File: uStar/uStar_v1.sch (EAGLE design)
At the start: 38 parts, among them IC1 INA138, X1 BU-SMA-V

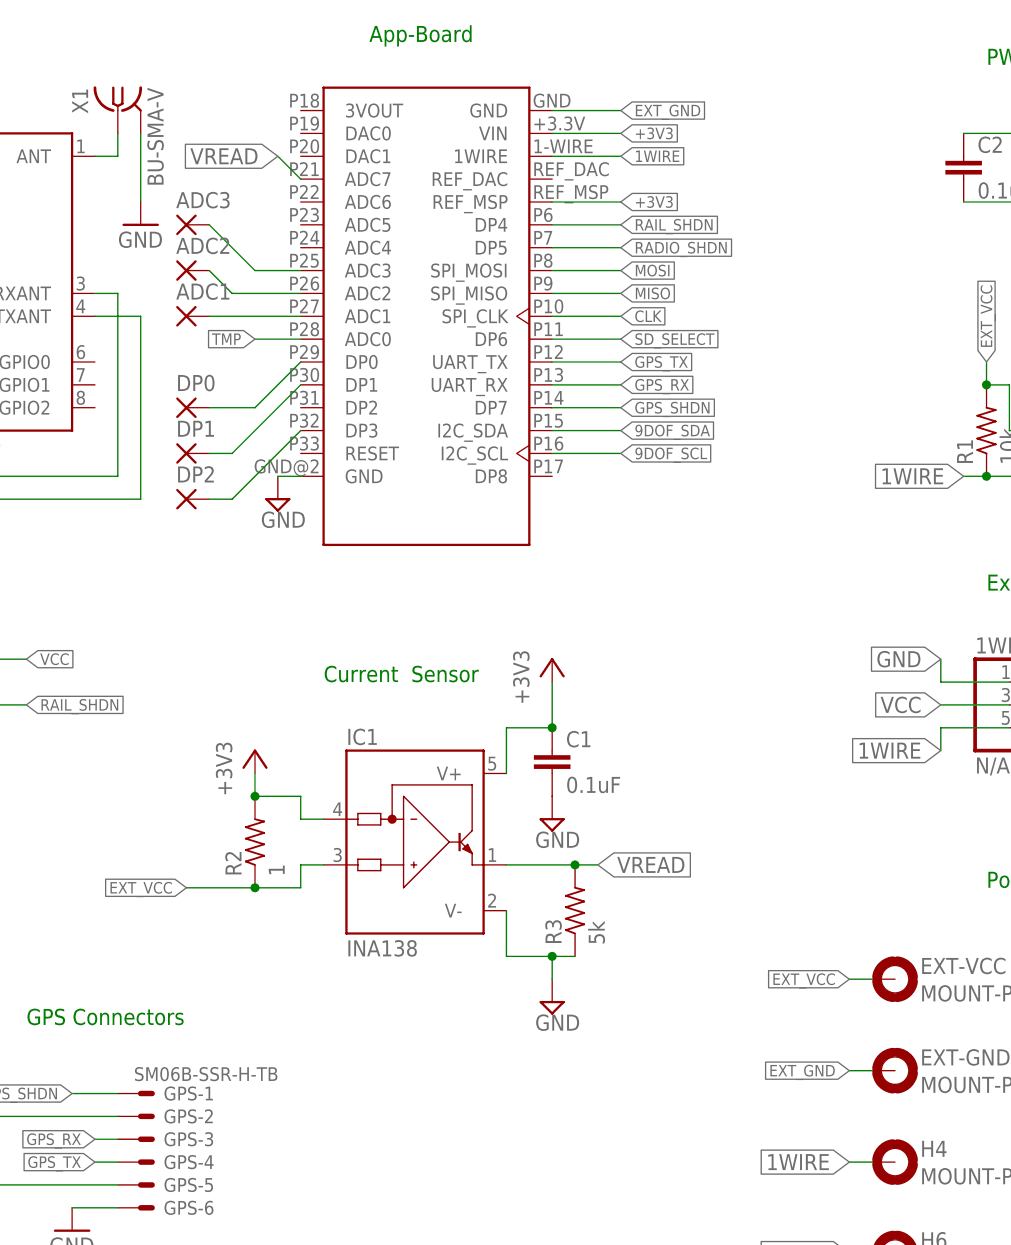
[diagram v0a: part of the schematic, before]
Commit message: added ADC lines instead of the uneeded ground
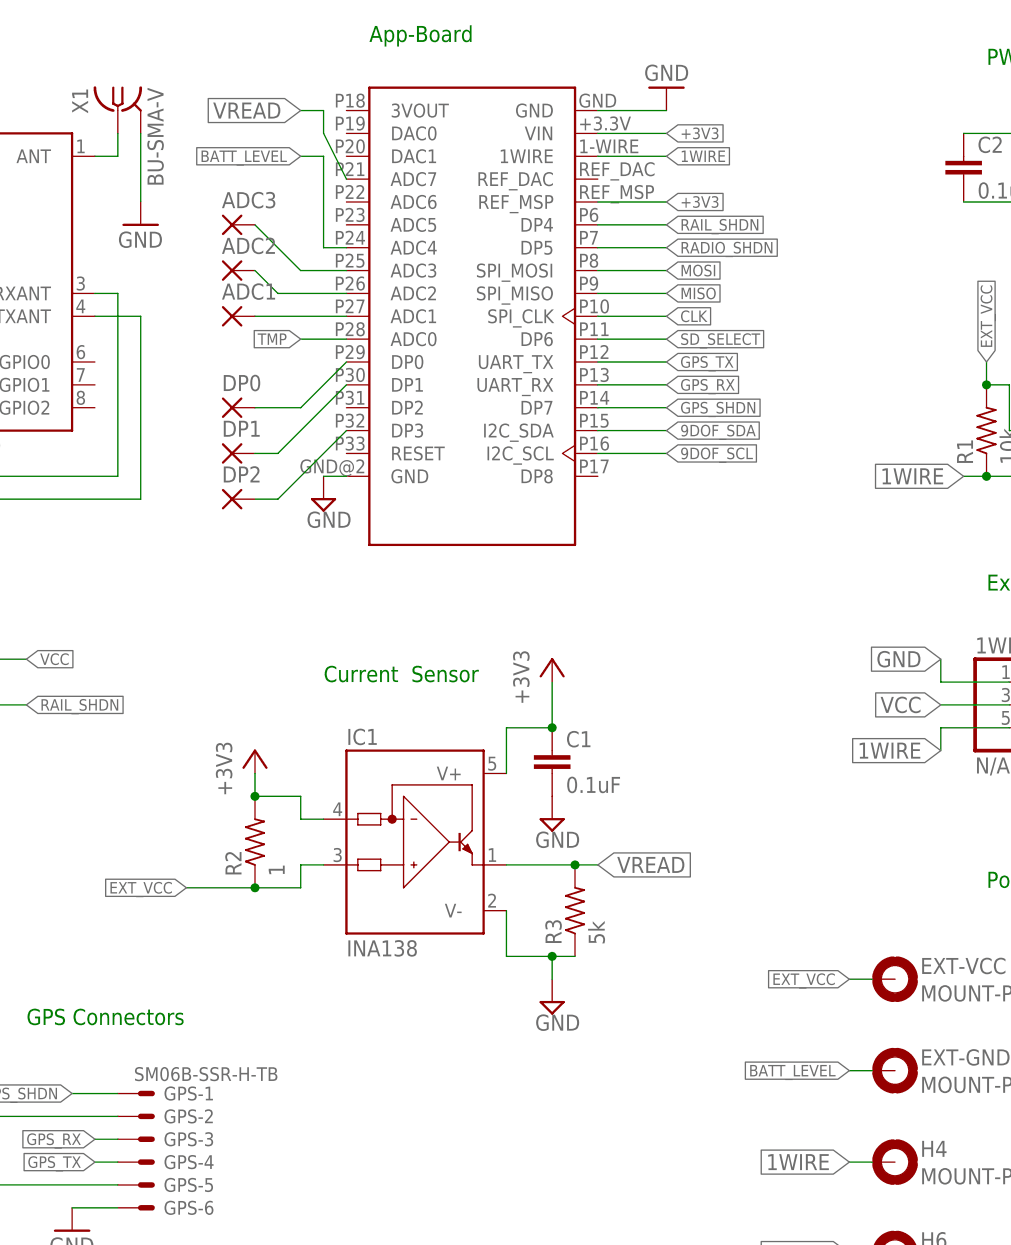
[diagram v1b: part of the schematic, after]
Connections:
- removed net EXT_GND: EXT-GND.MOUNT, U$1.GND@1
- new net BATT_LEVEL: EXT-GND.MOUNT, U$1.ADC4
- net GND: now also U$1.GND@1
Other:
- moved on the sheet: ADC1, ADC2, ADC3, DP0, DP1, DP2

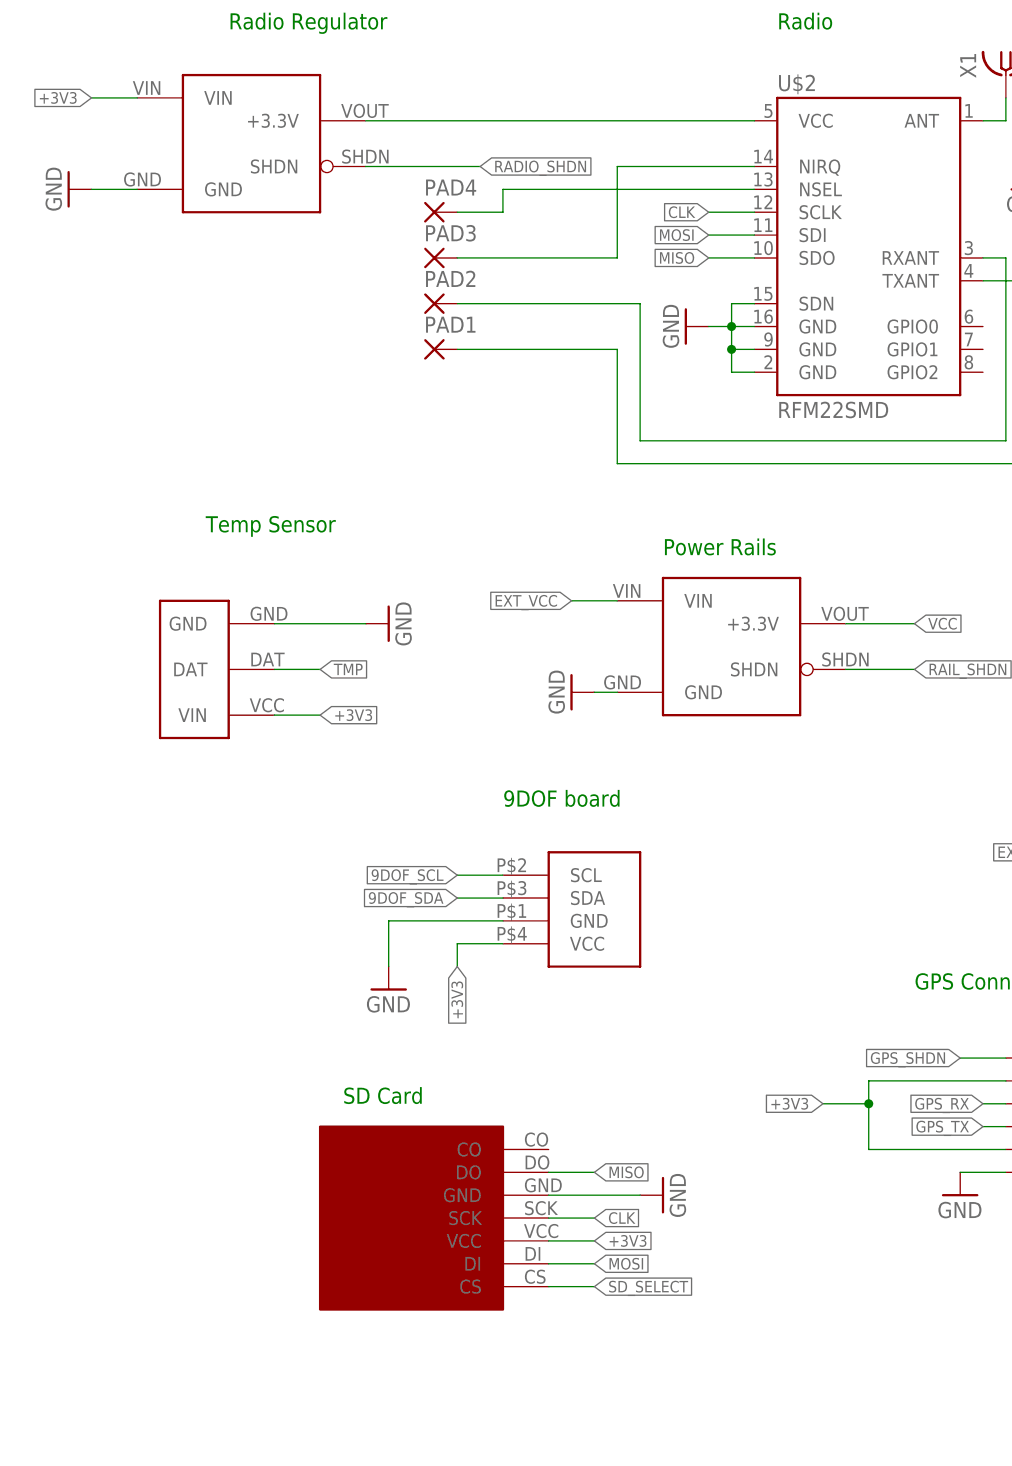
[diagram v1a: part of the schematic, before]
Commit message: fixed clearance violations
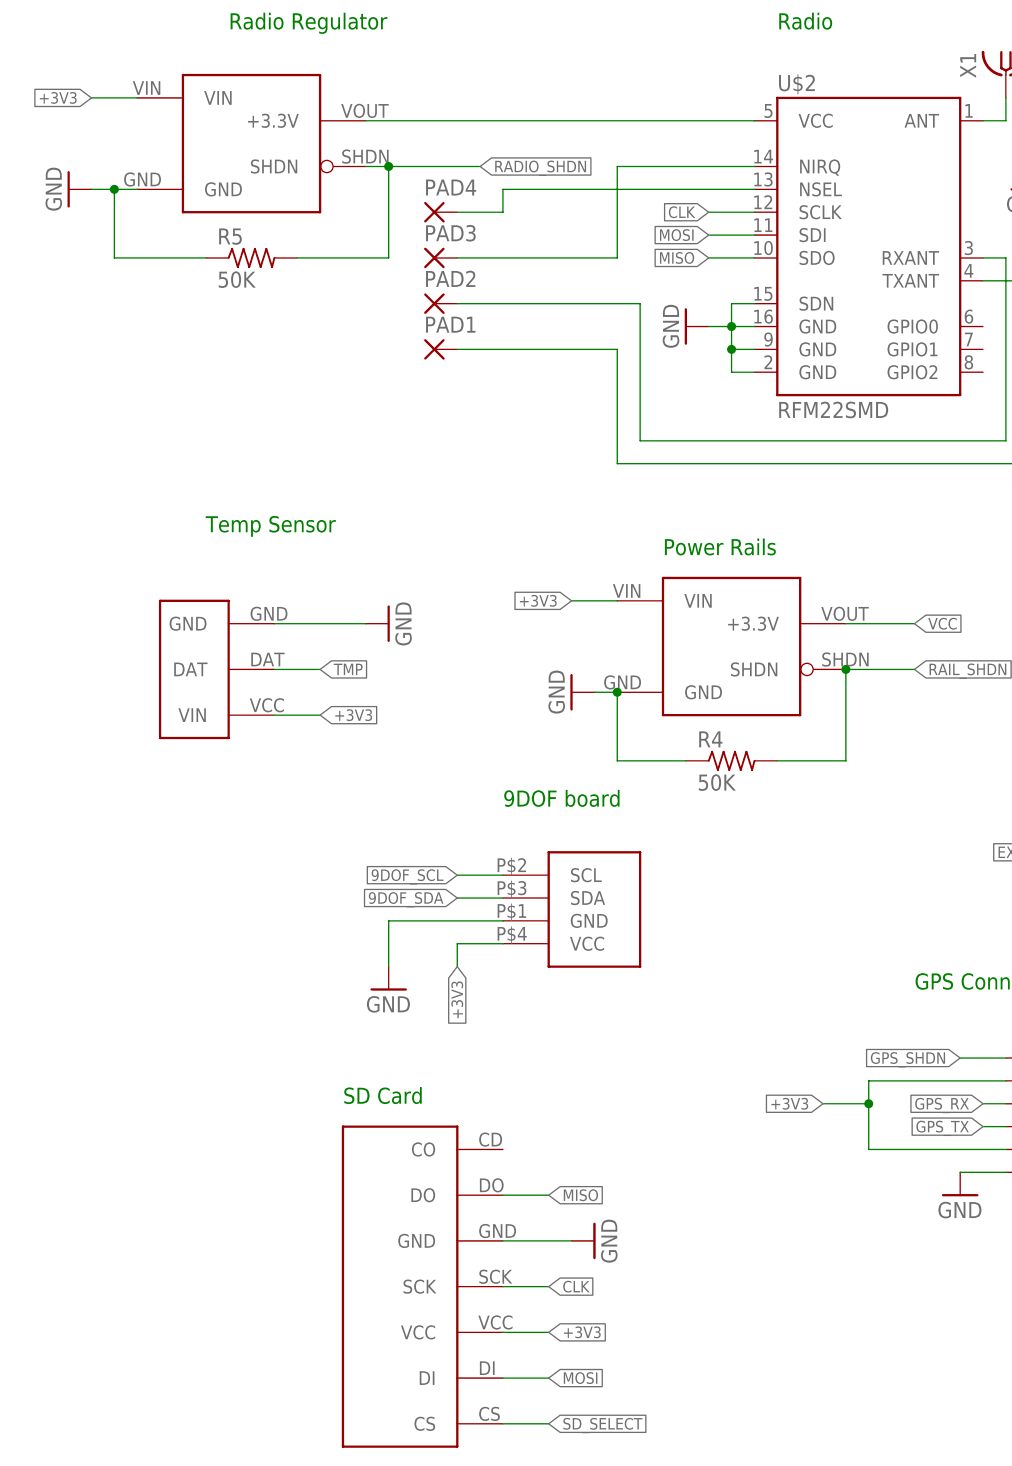
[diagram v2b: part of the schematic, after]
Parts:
- added R4, R5: 50K, rcl:R-US_R0603
- U$6: value BOB-00544 -> SDCARD_EXT; device LearningByMaking:BOB-00544 -> LearningByMaking:SDCARD_EXT
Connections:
- net +3V3: now also U$7.VIN
- net EXT_VCC: no longer U$7.VIN
- net GND: now also R4.1, R5.1
- net RADIO_SHDN: now also R5.2
- net RAIL_SHDN: now also R4.2
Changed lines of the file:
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@@
 <part name="PAD3" library="wirepad" deviceset="1,6/0,9" device="" value=" "/>
 <part name="PAD4" library="wirepad" deviceset="1,6/0,9" device="" value=" "/>
-<part name="U$6" library="LearningByMaking" deviceset="BOB-00544" device=""/>
 <part name="GND7" library="SparkFun-Aesthetics" deviceset="GND" device=""/>
 <part name="U$7" library="Pololu" deviceset="S7V8F3_VOLT_REG-3V3_1A" device="HORZ-DOWN"/>
@@
 <part name="DP2" library="wirepad" deviceset="1,6/0,9" device="" value=" "/>
 <part name="GND9" library="SparkFun-Aesthetics" deviceset="GND" device=""/>
+<part name="U$6" library="LearningByMaking" deviceset="SDCARD_EXT" device=""/>
+<part name="R4" library="rcl" deviceset="R-US_" device="R0603" value="50K"/>
+<part name="R5" library="rcl" deviceset="R-US_" device="R0603" value="50K"/>
 </parts>
 <sheets>
@@
 <instance part="PAD3" gate="1" x="45.72" y="152.4"/>
 <instance part="PAD4" gate="1" x="45.72" y="157.48"/>
-<instance part="U$6" gate="G$1" x="63.5" y="55.88"/>
-<instance part="GND7" gate="1" x="71.12" y="48.26" rot="R90"/>
+<instance part="GND7" gate="1" x="63.5" y="43.18" rot="R90"/>
 <instance part="U$7" gate="G$1" x="78.74" y="109.22"/>
 <instance part="GND8" gate="1" x="60.96" y="104.14" rot="R270"/>
@@
 <instance part="DP2" gate="1" x="121.92" y="129.54"/>
 <instance part="GND9" gate="1" x="170.18" y="175.26" rot="R180"/>
+<instance part="U$6" gate="G$1" x="53.34" y="38.1" rot="R90"/>
+<instance part="R4" gate="G$1" x="78.74" y="96.52"/>
+<instance part="R5" gate="G$1" x="25.4" y="152.4"/>
 </instances>
 <busses>
@@
 <pinref part="GND3" gate="1" pin="GND"/>
 <pinref part="U$3" gate="G$1" pin="GND"/>
-<wire x1="7.62" y1="160.02" x2="12.7" y2="160.02" width="0.1524" layer="91"/>
+<wire x1="7.62" y1="160.02" x2="10.16" y2="160.02" width="0.1524" layer="91"/>
+<pinref part="R5" gate="G$1" pin="1"/>
+<wire x1="10.16" y1="160.02" x2="12.7" y2="160.02" width="0.1524" layer="91"/>
+<wire x1="20.32" y1="152.4" x2="10.16" y2="152.4" width="0.1524" layer="91"/>
+<wire x1="10.16" y1="152.4" x2="10.16" y2="160.02" width="0.1524" layer="91"/>
+<junction x="10.16" y="160.02"/>
 </segment>
 <segment>
@@
 </segment>
 <segment>
+<pinref part="GND7" gate="1" pin="GND"/>
+<wire x1="53.34" y1="43.18" x2="60.96" y2="43.18" width="0.1524" layer="91"/>
 <pinref part="U$6" gate="G$1" pin="GND"/>
-<pinref part="GND7" gate="1" pin="GND"/>
-<wire x1="58.42" y1="48.26" x2="68.58" y2="48.26" width="0.1524" layer="91"/>
 </segment>
 <segment>
@@
 <pinref part="GND8" gate="1" pin="GND"/>
 <wire x1="66.04" y1="104.14" x2="63.5" y2="104.14" width="0.1524" layer="91"/>
+<pinref part="R4" gate="G$1" pin="1"/>
+<wire x1="73.66" y1="96.52" x2="66.04" y2="96.52" width="0.1524" layer="91"/>
+<wire x1="66.04" y1="96.52" x2="66.04" y2="104.14" width="0.1524" layer="91"/>
+<junction x="66.04" y="104.14"/>
 </segment>
 <segment>
@@
 </segment>
 <segment>
+<wire x1="53.34" y1="33.02" x2="58.42" y2="33.02" width="0.1524" layer="91"/>
+<label x="58.42" y="33.02" size="1.27" layer="95" xref="yes"/>
 <pinref part="U$6" gate="G$1" pin="VCC"/>
-<wire x1="58.42" y1="43.18" x2="63.5" y2="43.18" width="0.1524" layer="91"/>
-<label x="63.5" y="43.18" size="1.27" layer="95" xref="yes"/>
 </segment>
 <segment>
@@
 <label x="33.02" y="101.6" size="1.27" layer="95" xref="yes"/>
 <pinref part="U$4" gate="G$1" pin="VIN"/>
+</segment>
+<segment>
+<pinref part="U$7" gate="G$1" pin="VIN"/>
+<wire x1="66.04" y1="114.3" x2="60.96" y2="114.3" width="0.1524" layer="91"/>
+<label x="60.96" y="114.3" size="1.27" layer="95" rot="R180" xref="yes"/>
 </segment>
 </net>
@@
 </segment>
 <segment>
+<wire x1="53.34" y1="27.94" x2="58.42" y2="27.94" width="0.1524" layer="91"/>
+<label x="58.42" y="27.94" size="1.27" layer="95" xref="yes"/>
 <pinref part="U$6" gate="G$1" pin="DI"/>
-<wire x1="58.42" y1="40.64" x2="63.5" y2="40.64" width="0.1524" layer="91"/>
-<label x="63.5" y="40.64" size="1.27" layer="95" xref="yes"/>
 </segment>
 </net>
@@
 </segment>
 <segment>
+<wire x1="53.34" y1="48.26" x2="58.42" y2="48.26" width="0.1524" layer="91"/>
+<label x="58.42" y="48.26" size="1.27" layer="95" xref="yes"/>
 <pinref part="U$6" gate="G$1" pin="DO"/>
-<wire x1="58.42" y1="50.8" x2="63.5" y2="50.8" width="0.1524" layer="91"/>
-<label x="63.5" y="50.8" size="1.27" layer="95" xref="yes"/>
 </segment>
 </net>
@@
 </segment>
 <segment>
+<wire x1="53.34" y1="38.1" x2="58.42" y2="38.1" width="0.1524" layer="91"/>
+<label x="58.42" y="38.1" size="1.27" layer="95" xref="yes"/>
 <pinref part="U$6" gate="G$1" pin="SCK"/>
-<wire x1="58.42" y1="45.72" x2="63.5" y2="45.72" width="0.1524" layer="91"/>
-<label x="63.5" y="45.72" size="1.27" layer="95" xref="yes"/>
 </segment>
 </net>
@@
 <segment>
 <pinref part="U$3" gate="G$1" pin="SHDN"/>
-<wire x1="38.1" y1="162.56" x2="50.8" y2="162.56" width="0.1524" layer="91"/>
+<wire x1="38.1" y1="162.56" x2="40.64" y2="162.56" width="0.1524" layer="91"/>
 <label x="50.8" y="162.56" size="1.27" layer="95" xref="yes"/>
+<pinref part="R5" gate="G$1" pin="2"/>
+<wire x1="40.64" y1="162.56" x2="50.8" y2="162.56" width="0.1524" layer="91"/>
+<wire x1="30.48" y1="152.4" x2="40.64" y2="152.4" width="0.1524" layer="91"/>
+<wire x1="40.64" y1="152.4" x2="40.64" y2="162.56" width="0.1524" layer="91"/>
+<junction x="40.64" y="162.56"/>
 </segment>
 <segment>
@@
 <net name="SD_SELECT" class="0">
 <segment>
+<wire x1="53.34" y1="22.86" x2="58.42" y2="22.86" width="0.1524" layer="91"/>
+<label x="58.42" y="22.86" size="1.27" layer="95" xref="yes"/>
 <pinref part="U$6" gate="G$1" pin="CS"/>
-<wire x1="58.42" y1="38.1" x2="63.5" y2="38.1" width="0.1524" layer="91"/>
-<label x="63.5" y="38.1" size="1.27" layer="95" xref="yes"/>
 </segment>
 <segment>
@@
 </net>
 <net name="EXT_VCC" class="0">
-<segment>
-<pinref part="U$7" gate="G$1" pin="VIN"/>
-<wire x1="66.04" y1="114.3" x2="60.96" y2="114.3" width="0.1524" layer="91"/>
-<label x="60.96" y="114.3" size="1.27" layer="95" rot="R180" xref="yes"/>
-</segment>
 <segment>
 <wire x1="193.04" y1="76.2" x2="190.5" y2="76.2" width="0.1524" layer="91"/>
@@
 <wire x1="91.44" y1="106.68" x2="99.06" y2="106.68" width="0.1524" layer="91"/>
 <label x="99.06" y="106.68" size="1.27" layer="95" xref="yes"/>
-</segment>
-</net>
+<pinref part="R4" gate="G$1" pin="2"/>
+<wire x1="83.82" y1="96.52" x2="91.44" y2="96.52" width="0.1524" layer="91"/>
+<wire x1="91.44" y1="96.52" x2="91.44" y2="106.68" width="0.1524" layer="91"/>
+<junction x="91.44" y="106.68"/>
+</segment>
+</net>
